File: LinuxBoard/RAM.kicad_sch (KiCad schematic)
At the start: 20 parts, among them J5 Conn_ARM_JTAG_SWD_10, SW4 SW_Push, U1 STM32MP151AAB3, U2 MT41K64M16TW-107_AAT_J_TR

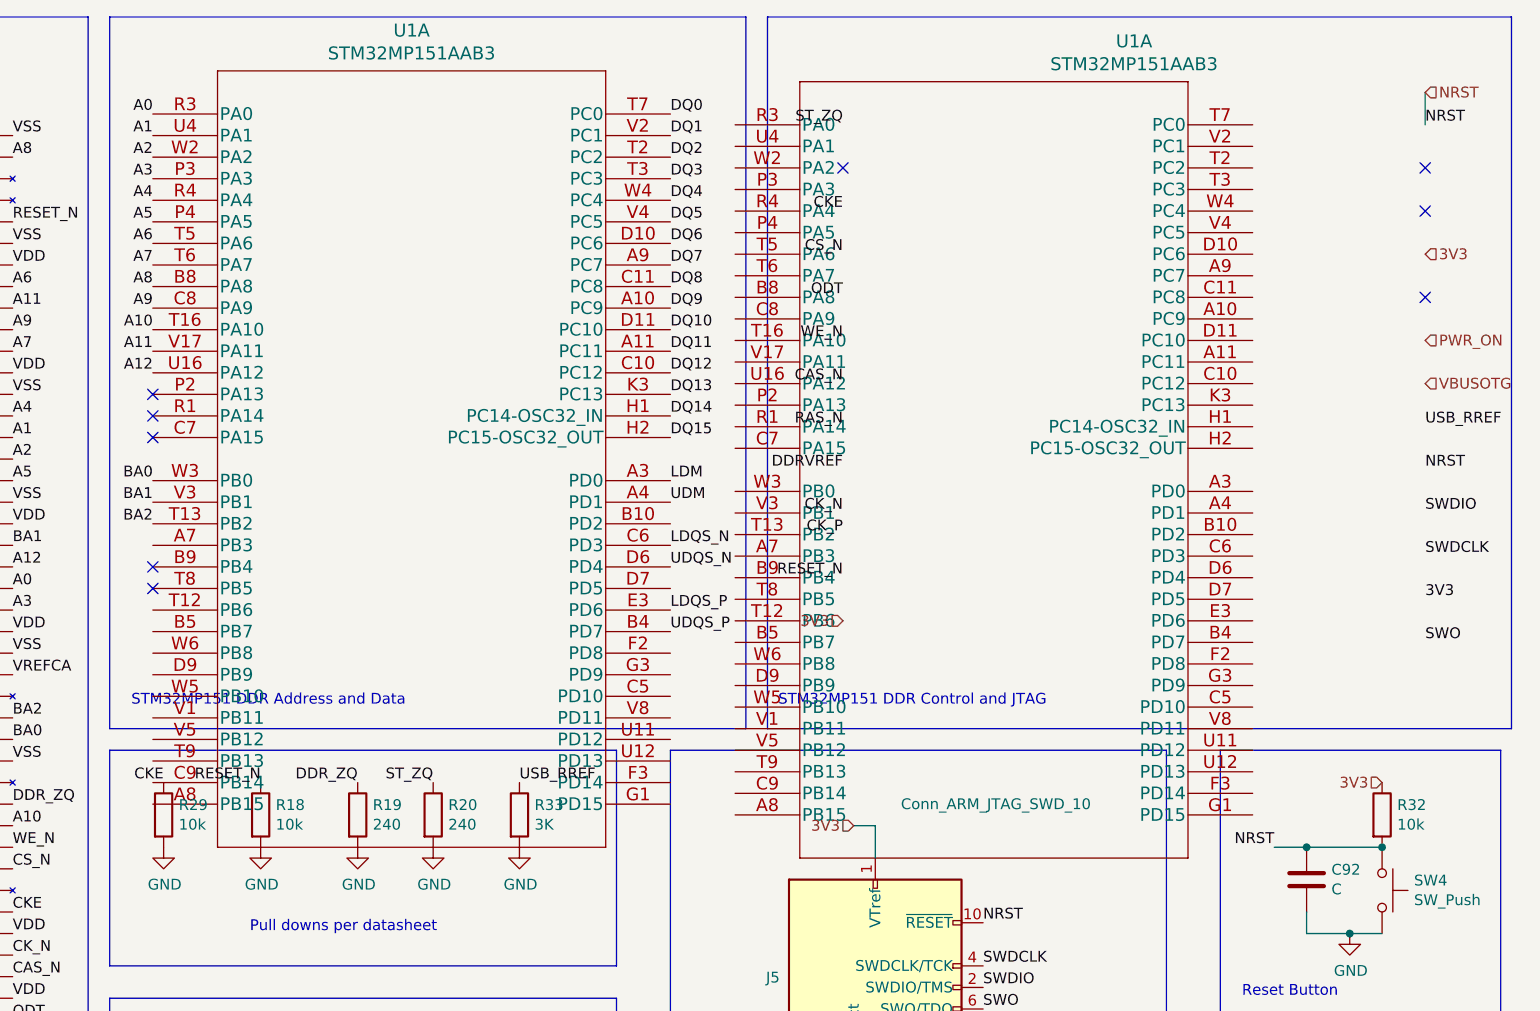
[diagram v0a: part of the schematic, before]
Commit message: Fix ERC errors and reorganize directory
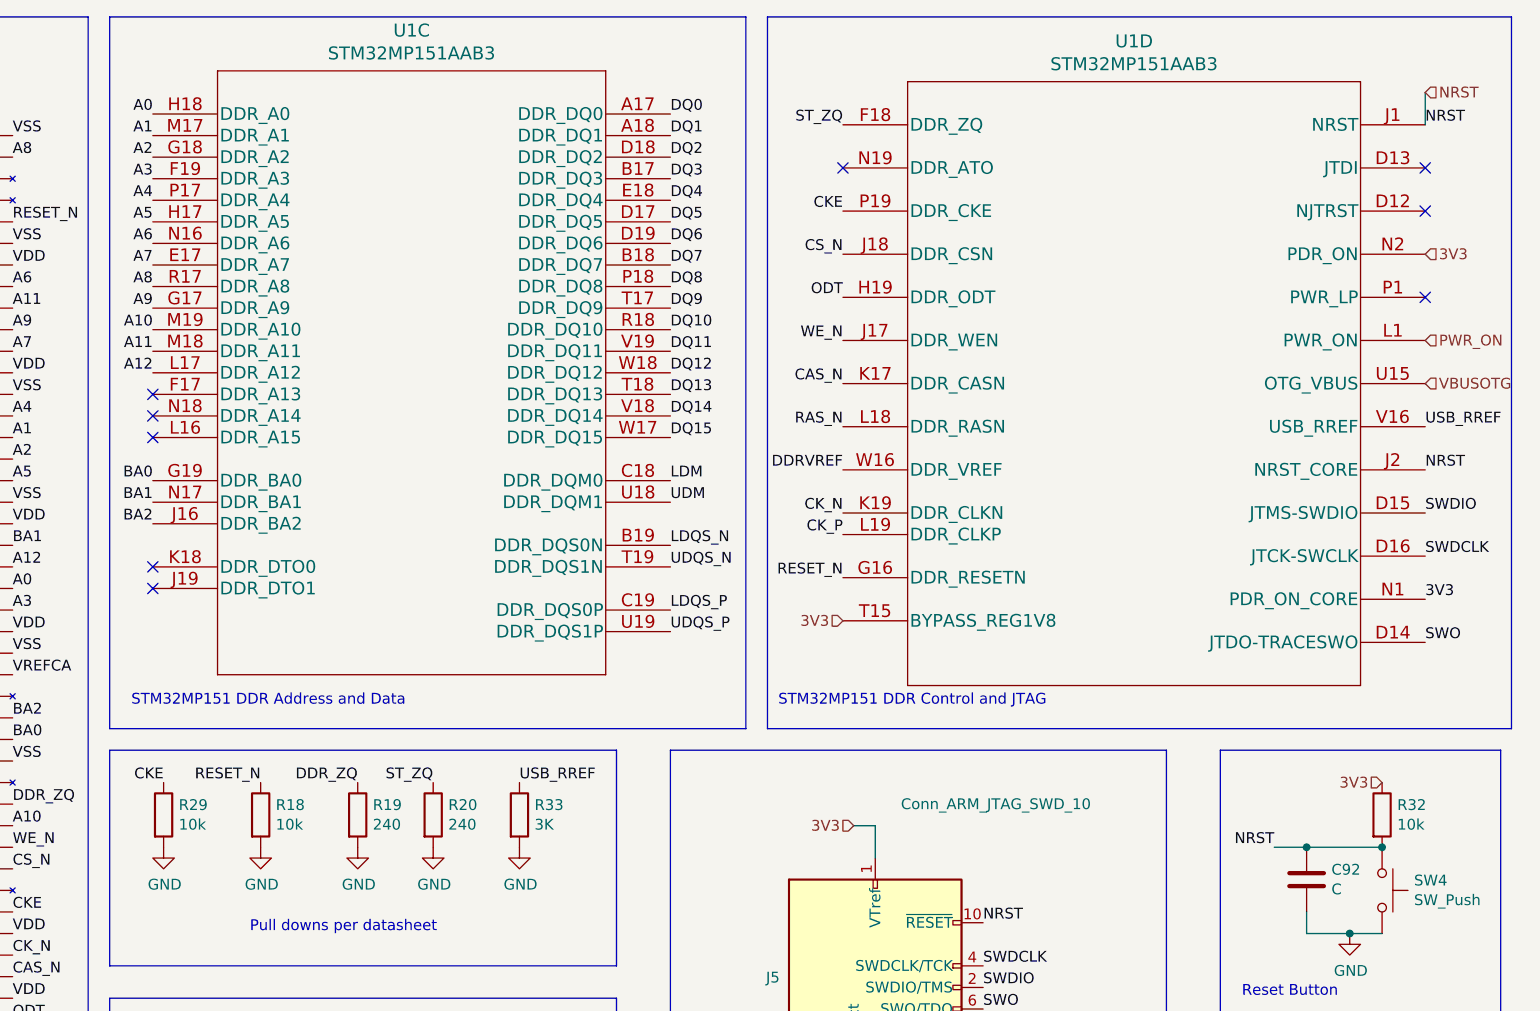
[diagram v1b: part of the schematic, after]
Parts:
- R33: footprint Resistor_SMD:R_0603_1608Metric -> Resistor_SMD:R_0603_1608Metric_Pad0.98x0.95mm_HandSolder
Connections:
- net 3V3: now also U1.N1 (PDR_ON_CORE), U1.N2 (PDR_ON), U1.T15 (BYPASS_REG1V8)
- net A0: now also U1.H18 (DDR_A0); no longer U1.R3 (PA0)
- net A1: now also U1.M17 (DDR_A1); no longer U1.U4 (PA1)
- net A10: now also U1.M19 (DDR_A10); no longer U1.T16 (PA10)
- net A11: now also U1.M18 (DDR_A11); no longer U1.V17 (PA11)
- net A12: now also U1.L17 (DDR_A12); no longer U1.U16 (PA12)
- net A2: now also U1.G18 (DDR_A2); no longer U1.W2 (PA2)
- net A3: now also U1.F19 (DDR_A3); no longer U1.P3 (PA3)
- net A4: now also U1.P17 (DDR_A4); no longer U1.R4 (PA4)
- net A5: now also U1.H17 (DDR_A5); no longer U1.P4 (PA5)
- net A6: now also U1.N16 (DDR_A6); no longer U1.T5 (PA6)
- net A7: now also U1.E17 (DDR_A7); no longer U1.T6 (PA7)
- net A8: now also U1.R17 (DDR_A8); no longer U1.B8 (PA8)
- net A9: now also U1.G17 (DDR_A9); no longer U1.C8 (PA9)
- net BA0: now also U1.G19 (DDR_BA0); no longer U1.W3 (PB0)
- net BA1: now also U1.N17 (DDR_BA1); no longer U1.V3 (PB1)
- net BA2: now also U1.J16 (DDR_BA2); no longer U1.T13 (PB2)
- net CAS_N: now also U1.K17 (DDR_CASN)
- net CKE: now also U1.P19 (DDR_CKE)
- net CK_N: now also U1.K19 (DDR_CLKN)
- net CK_P: now also U1.L19 (DDR_CLKP)
- net CS_N: now also U1.J18 (DDR_CSN)
- net DQ0: now also U1.A17 (DDR_DQ0); no longer U1.T7 (PC0)
- net DQ1: now also U1.A18 (DDR_DQ1); no longer U1.V2 (PC1)
- net DQ10: now also U1.R18 (DDR_DQ10); no longer U1.D11 (PC10)
- net DQ11: now also U1.V19 (DDR_DQ11); no longer U1.A11 (PC11)
- net DQ12: now also U1.W18 (DDR_DQ12); no longer U1.C10 (PC12)
- net DQ13: now also U1.T18 (DDR_DQ13); no longer U1.K3 (PC13)
- net DQ14: now also U1.V18 (DDR_DQ14); no longer U1.H1 (PC14-OSC32_IN)
- net DQ15: now also U1.W17 (DDR_DQ15); no longer U1.H2 (PC15-OSC32_OUT)
- net DQ2: now also U1.D18 (DDR_DQ2); no longer U1.T2 (PC2)
- net DQ3: now also U1.B17 (DDR_DQ3); no longer U1.T3 (PC3)
- net DQ4: now also U1.E18 (DDR_DQ4); no longer U1.W4 (PC4)
- net DQ5: now also U1.D17 (DDR_DQ5); no longer U1.V4 (PC5)
- net DQ6: now also U1.D19 (DDR_DQ6); no longer U1.D10 (PC6)
- net DQ7: now also U1.B18 (DDR_DQ7); no longer U1.A9 (PC7)
- net DQ8: now also U1.P18 (DDR_DQ8); no longer U1.C11 (PC8)
- net DQ9: now also U1.T17 (DDR_DQ9); no longer U1.A10 (PC9)
- net LDM: now also U1.C18 (DDR_DQM0); no longer U1.A3 (PD0)
- net LDQS_N: now also U1.B19 (DDR_DQS0N); no longer U1.C6 (PD3)
- net LDQS_P: now also U1.C19 (DDR_DQS0P); no longer U1.E3 (PD6)
- net NRST: now also U1.J1 (NRST), U1.J2 (NRST_CORE)
- net ODT: now also U1.H19 (DDR_ODT)
- net PMIC_DDR_VREF: now also U1.W16 (DDR_VREF)
- net PWR_ON: now also U1.L1 (PWR_ON)
- net RAS_N: now also U1.L18 (DDR_RASN)
- net RESET_N: now also U1.G16 (DDR_RESETN)
- net ST_ZQ: now also U1.F18 (DDR_ZQ)
- net SWDCLK: now also U1.D16 (JTCK-SWCLK)
- net SWDIO: now also U1.D15 (JTMS-SWDIO)
- net SWO: now also U1.D14 (JTDO-TRACESWO)
- net UDM: now also U1.U18 (DDR_DQM1); no longer U1.A4 (PD1)
- net UDQS_N: now also U1.T19 (DDR_DQS1N); no longer U1.D6 (PD4)
- net UDQS_P: now also U1.U19 (DDR_DQS1P); no longer U1.B4 (PD7)
- net USB_RREF: now also U1.V16 (USB_RREF)
- net VBUSOTG: now also U1.U15 (OTG_VBUS)
- net WE_N: now also U1.J17 (DDR_WEN)
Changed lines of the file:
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@@
     (pin "T9")
   )
-  (symbol (lib_id "LinuxBoard:STM32MP151AAB3") (at 191.77 29.21 0)
+  (symbol (lib_id "LinuxBoard:STM32MP151AAB3") (at 191.77 29.21 0) (unit 4)
     (in_bom yes) (on_board yes)
     (property "Reference" "U1" (id 0) (at 238.76 19.3802 0)
@@
     (pin "W16")
   )
-  (symbol (lib_id "LinuxBoard:STM32MP151AAB3") (at 123.19 27.94 0)
+  (symbol (lib_id "LinuxBoard:STM32MP151AAB3") (at 123.19 27.94 0) (unit 3)
     (in_bom yes) (on_board yes)
     (property "Reference" "U1" (id 0) (at 153.67 18.1102 0)
@@
       (effects (font (size 1.27 1.27)) (justify left))
     )
-    (property "Footprint" "Resistor_SMD:R_0603_1608Metric" (id 2) (at 164.592 110.49 90)
-      (effects (font (size 1.27 1.27)) hide)
-    )
+    (property "Footprint" "Resistor_SMD:R_0603_1608Metric_Pad0.98x0.95mm_HandSolder" (id 2) (at 164.592 110.49 90)
+      (effects (font (size 1.27 1.27)) hide)
+    )

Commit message: Fix resistor footprints, restart layout
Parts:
- R18, R29, R30, R32: footprint Resistor_SMD:R_0603_1608Metric_Pad1.05x0.95mm_HandSolder -> Resistor_SMD:R_0603_1608Metric_Pad0.98x0.95mm_HandSolder
- R19, R20: footprint Resistor_SMD:R_0603_1608Metric -> Resistor_SMD:R_0603_1608Metric_Pad0.98x0.95mm_HandSolder
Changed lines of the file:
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@@
       (effects (font (size 1.27 1.27)) (justify left))
     )
-    (property "Footprint" "Resistor_SMD:R_0603_1608Metric_Pad1.05x0.95mm_HandSolder" (id 2) (at 134.112 110.49 90)
+    (property "Footprint" "Resistor_SMD:R_0603_1608Metric_Pad0.98x0.95mm_HandSolder" (id 2) (at 134.112 110.49 90)
       (effects (font (size 1.27 1.27)) hide)
     )
@@
       (effects (font (size 1.27 1.27)) (justify left))
     )
-    (property "Footprint" "Resistor_SMD:R_0603_1608Metric" (id 2) (at 145.542 110.49 90)
+    (property "Footprint" "Resistor_SMD:R_0603_1608Metric_Pad0.98x0.95mm_HandSolder" (id 2) (at 145.542 110.49 90)
       (effects (font (size 1.27 1.27)) hide)
     )
@@
       (effects (font (size 1.27 1.27)) (justify left))
     )
-    (property "Footprint" "Resistor_SMD:R_0603_1608Metric" (id 2) (at 154.432 110.49 90)
+    (property "Footprint" "Resistor_SMD:R_0603_1608Metric_Pad0.98x0.95mm_HandSolder" (id 2) (at 154.432 110.49 90)
       (effects (font (size 1.27 1.27)) hide)
     )
@@
       (effects (font (size 1.27 1.27)) (justify left))
     )
-    (property "Footprint" "Resistor_SMD:R_0603_1608Metric_Pad1.05x0.95mm_HandSolder" (id 2) (at 266.192 110.49 90)
+    (property "Footprint" "Resistor_SMD:R_0603_1608Metric_Pad0.98x0.95mm_HandSolder" (id 2) (at 266.192 110.49 90)
       (effects (font (size 1.27 1.27)) hide)
     )
@@
       (effects (font (size 1.27 1.27)) (justify left))
     )
-    (property "Footprint" "Resistor_SMD:R_0603_1608Metric_Pad1.05x0.95mm_HandSolder" (id 2) (at 143.002 140.97 90)
+    (property "Footprint" "Resistor_SMD:R_0603_1608Metric_Pad0.98x0.95mm_HandSolder" (id 2) (at 143.002 140.97 90)
       (effects (font (size 1.27 1.27)) hide)
     )
@@
       (effects (font (size 1.27 1.27)) (justify left))
     )
-    (property "Footprint" "Resistor_SMD:R_0603_1608Metric_Pad1.05x0.95mm_HandSolder" (id 2) (at 122.682 110.49 90)
-      (effects (font (size 1.27 1.27)) hide)
-    )
+    (property "Footprint" "Resistor_SMD:R_0603_1608Metric_Pad0.98x0.95mm_HandSolder" (id 2) (at 122.682 110.49 90)
+      (effects (font (size 1.27 1.27)) hide)
+    )
